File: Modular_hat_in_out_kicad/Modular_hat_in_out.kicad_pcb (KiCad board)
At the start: 2 copper layers, 65 x 56 mm, 146 parts, among them J1 Raspberry_Pi_2_3, U1 MCP3008, U2 LM324, U3 MCP3008, U4 MCP4728, U5 MCP4728, U6 LM324

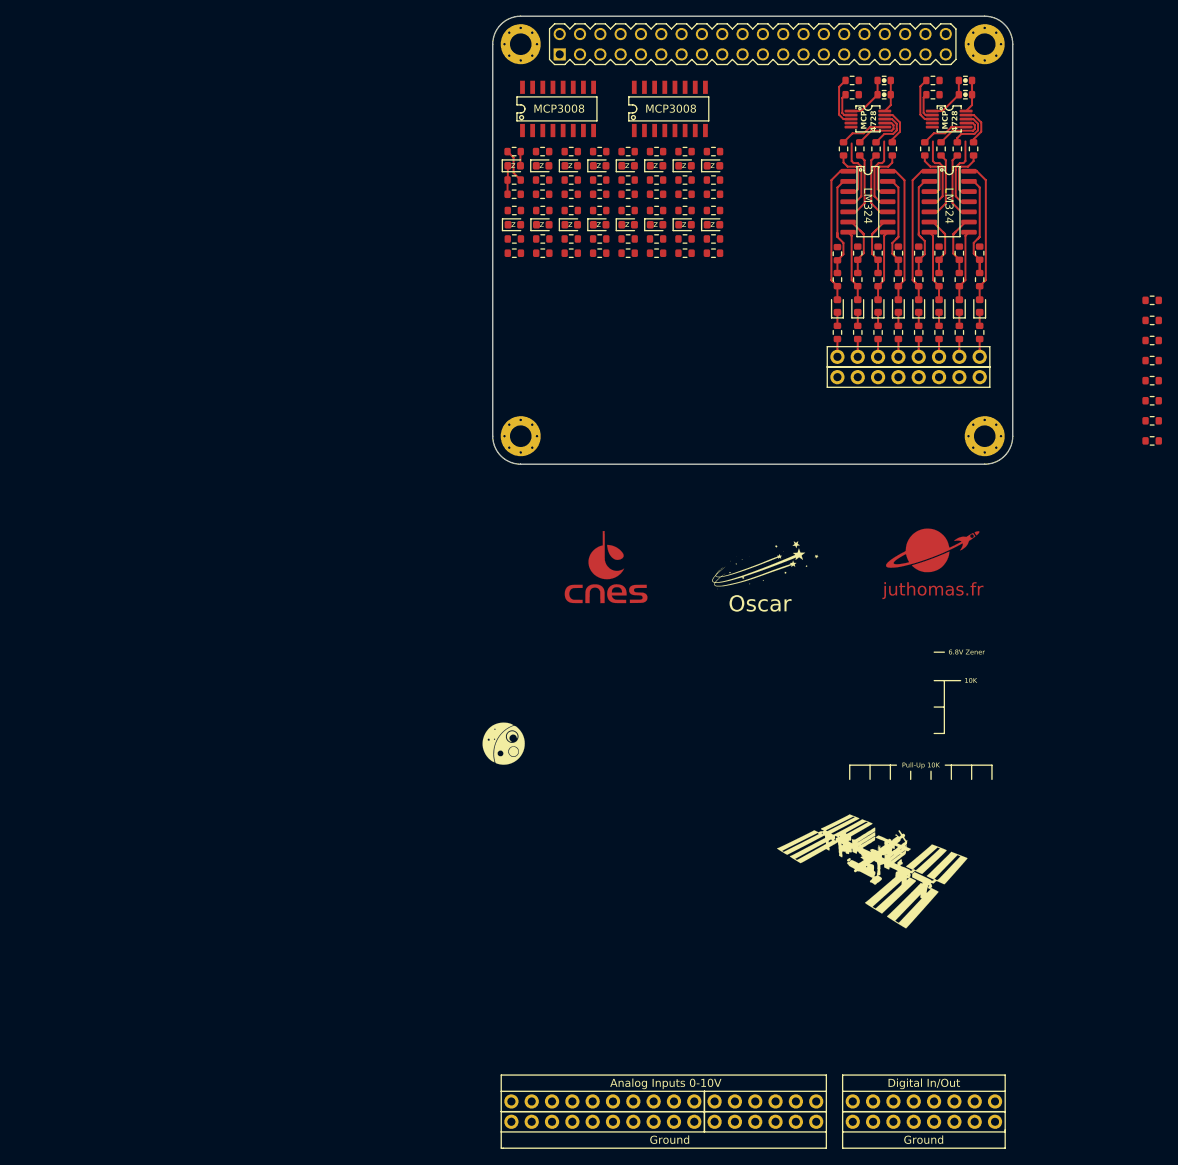
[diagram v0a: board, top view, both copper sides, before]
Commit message: [ADD] Some placements
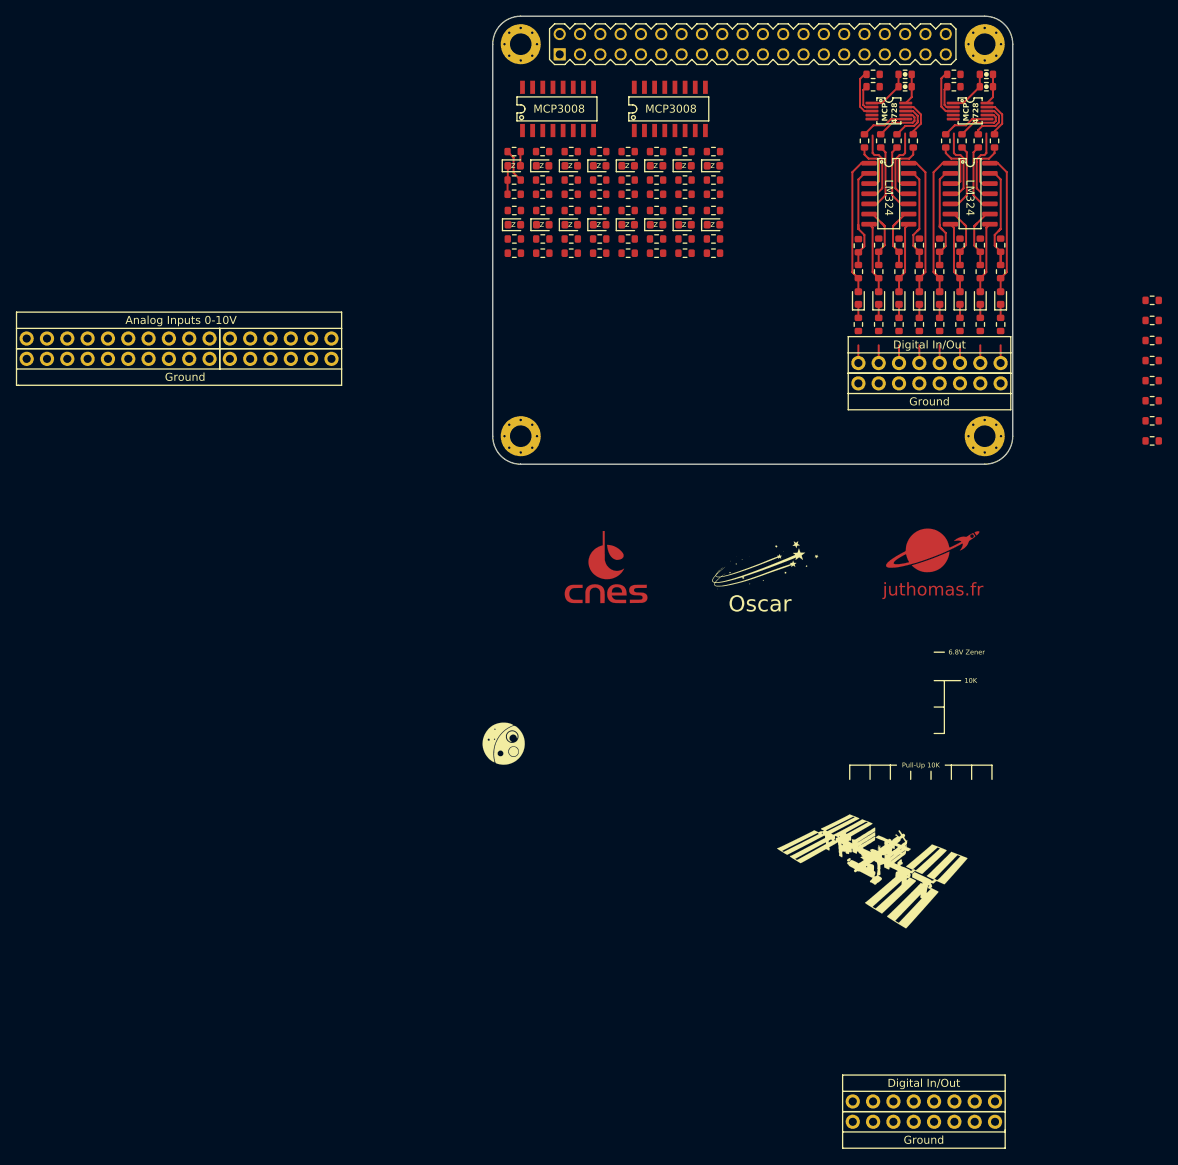
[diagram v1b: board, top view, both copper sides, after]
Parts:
- moved JP1 113.0 mm to (-1.05, 65.5)
- moved JP4 113.0 mm to (-21.4, 65.5)
- moved JP3 113.0 mm to (-1.05, 68.0)
- moved JP6 113.0 mm to (-21.4, 68.0)
- moved C1 2.80 mm to (77.0, 34.0)
- moved C3 2.80 mm to (87.2, 34.0)
- moved D18 2.80 mm to (73.7, 60.4)
- moved D19 2.80 mm to (76.2, 60.4)
- moved D21 2.80 mm to (81.3, 60.4)
- moved D23 2.80 mm to (86.4, 60.4)
- moved R60 2.80 mm to (73.7, 57.1)
- moved R61 2.80 mm to (73.7, 53.8)
- moved R62 2.80 mm to (74.0, 40.8)
- moved R66 2.80 mm to (76.2, 57.1)
- moved R67 2.80 mm to (76.2, 53.8)
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
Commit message: [ADD] Pre routing MCP3008
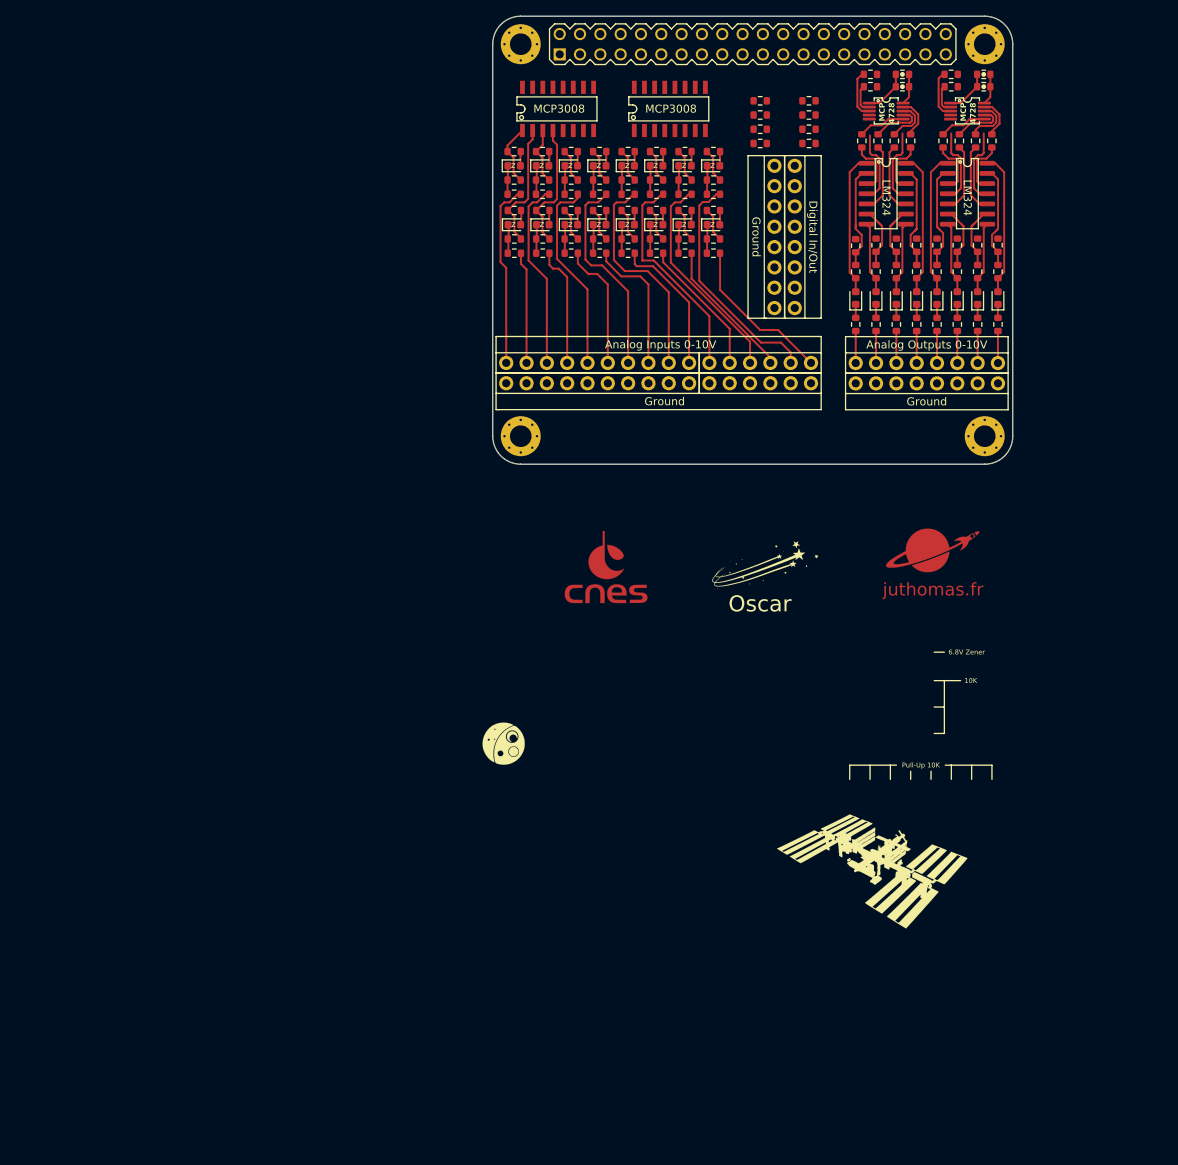
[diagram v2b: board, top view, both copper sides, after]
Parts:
- moved JP2 112.2 mm to (60.7, 52.8), turned to -90 degrees
- moved JP5 109.3 mm to (63.2, 52.8), turned to -90 degrees
- moved R56 63.7 mm to (58.9, 37.6), turned to 180 degrees
- moved R54 61.7 mm to (58.9, 35.8), turned to 180 degrees
- moved JP1 60.0 mm to (58.9, 68.5)
- moved JP3 60.0 mm to (58.9, 71.1)
- moved JP4 60.0 mm to (38.6, 68.5)
- moved JP6 60.0 mm to (38.6, 71.1)
- moved R55 57.5 mm to (65.0, 37.6)
- moved R52 56.0 mm to (58.9, 41.1), turned to 180 degrees
- moved R53 55.4 mm to (65.0, 35.8)
- moved R50 54.5 mm to (58.9, 39.3), turned to 180 degrees
- moved R51 49.5 mm to (65.0, 41.1)
- moved R4 47.9 mm to (65.0, 39.3)
- moved C1 0.33 mm to (76.7, 34.0)
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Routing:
- net /RG14: track 0.00 -> 29.0 mm
- net /RG8: track 0.00 -> 27.4 mm
- net /RG10: track 0.00 -> 27.2 mm
- net /RG12: track 0.00 -> 26.9 mm
- net GND: track 29.1 -> 55.2 mm
- net /RG6: track 0.00 -> 25.9 mm
- net /RG4: track 0.00 -> 24.7 mm
- net /RG2: track 0.00 -> 23.7 mm
- net /RG0: track 0.00 -> 23.0 mm
- net /RG15: track 0.00 -> 19.7 mm
- net /RG13: track 0.00 -> 17.8 mm
- net /RG9: track 0.00 -> 17.7 mm
- net /RG7: track 0.00 -> 17.3 mm
- net /RG11: track 0.00 -> 17.2 mm
- net /CH3: track 0.00 -> 16.2 mm
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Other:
- board text added: "Analog Outputs 0-10V"

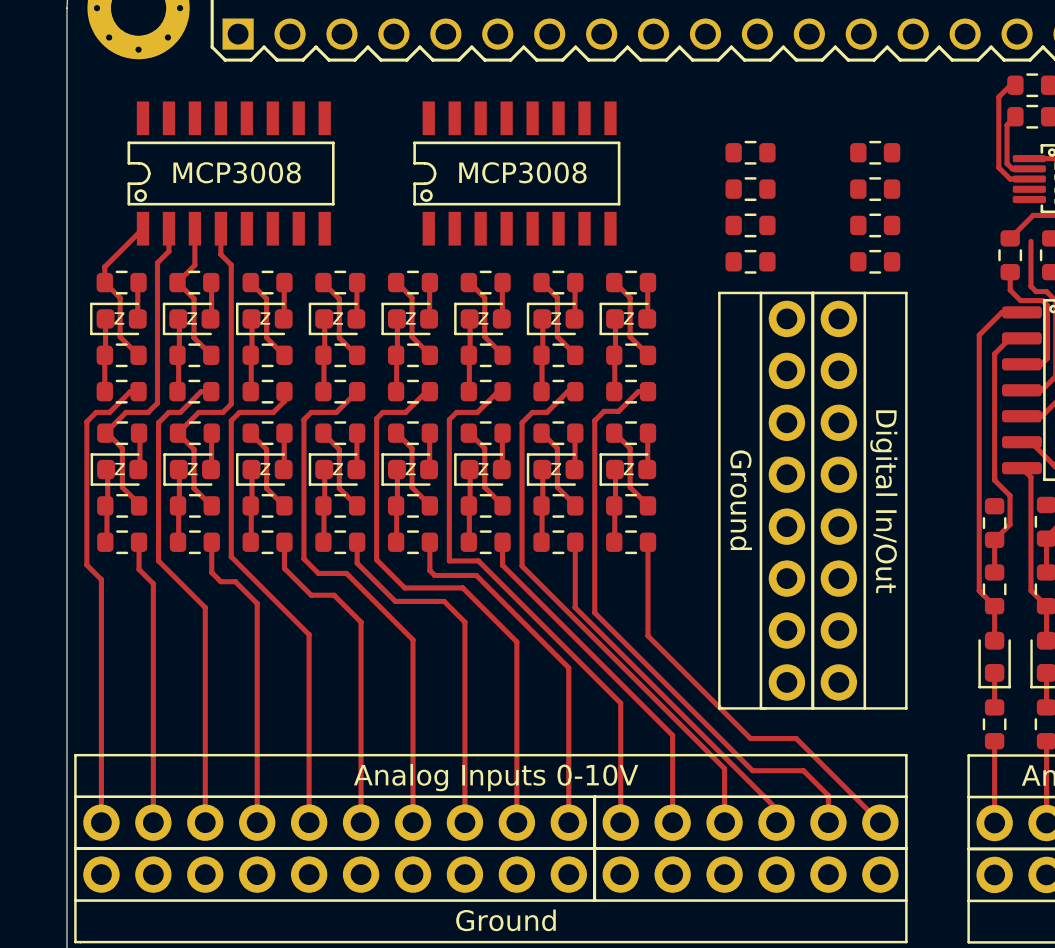
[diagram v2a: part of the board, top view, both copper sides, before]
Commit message: [ADD] Digital routing
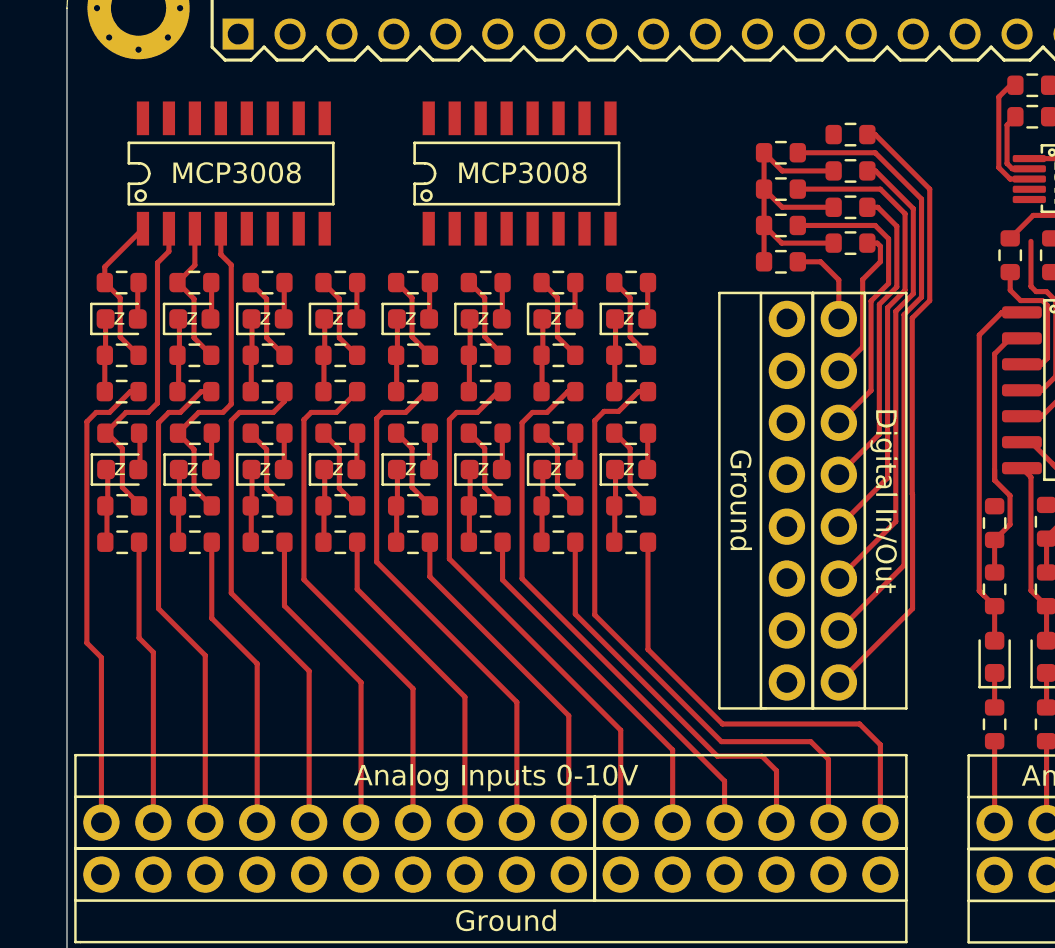
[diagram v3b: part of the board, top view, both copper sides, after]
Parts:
- moved R51 1.51 mm to (63.8, 40.2), turned to 180 degrees
- moved R4 1.50 mm to (63.8, 38.4), turned to 180 degrees
- moved R53 1.50 mm to (63.8, 34.9), turned to 180 degrees
- moved R55 1.50 mm to (63.8, 36.7), turned to 180 degrees
- moved R50 1.49 mm to (60.4, 39.3)
- moved R52 1.49 mm to (60.4, 41.1)
- moved R54 1.49 mm to (60.4, 35.8)
- moved R56 1.49 mm to (60.4, 37.6)
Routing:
- net /D8: track 0.00 -> 30.1 mm
- net /D7: track 0.00 -> 29.8 mm
- net /D6: track 0.00 -> 22.6 mm
- net /D5: track 0.00 -> 22.4 mm
- net /3V3_REG: track 0.00 -> 16.6 mm
- net /D4: track 0.00 -> 15.2 mm
- net /D3: track 0.00 -> 14.7 mm
- net /D2: track 0.00 -> 7.64 mm
- net /D1: track 0.00 -> 4.28 mm
- net /RG15: track 19.7 -> 22.4 mm
- net /RG8: track 27.4 -> 25.8 mm
- net /RG7: track 17.3 -> 15.9 mm
- net /RG13: track 17.8 -> 19.1 mm
- net /RG9: track 17.7 -> 16.5 mm
- net /RG14: track 29.0 -> 30.1 mm
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
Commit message: [ADD] Routing digital
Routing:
- net /GPIO3: track 7.28 -> 83.5 mm
- net /GPIO2: track 12.6 -> 85.6 mm
- net +5V: track 11.9 -> 81.4 mm, vias 0 -> 2
- net /D8: track 30.1 -> 75.1 mm, vias 0 -> 2
- net /D7: track 29.8 -> 72.8 mm, vias 0 -> 2
- net /3V3_REG: track 16.6 -> 58.8 mm, vias 0 -> 2
- net /GPIO11: track 0.00 -> 37.1 mm
- net /D6: track 22.6 -> 57.4 mm
- net /GPIO9: track 0.00 -> 33.6 mm
- net /D5: track 22.4 -> 55.2 mm
- net /GPIO8: track 0.00 -> 28.9 mm
- net /GPIO10: track 0.00 -> 28.7 mm
- net /D4: track 15.2 -> 43.5 mm
- net /D3: track 14.7 -> 39.1 mm
- net /D2: track 7.64 -> 27.7 mm
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
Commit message: [ADD] 12V input in shematics
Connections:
- J1 pad 22: unconnected-(J1-GPIO25-Pad22) -> /GPIO25
- J1 pad 27: unconnected-(J1-ID_SD/GPIO0-Pad27) -> /GPIO0
- J1 pad 28: unconnected-(J1-ID_SC/GPIO1-Pad28) -> /GPIO1
- J1 pad 40: unconnected-(J1-GPIO21/SCLK1-Pad40) -> /GPIO20
- U4 pad 4: Net-(U4-~{LDAC}) -> /GPIO0
- U4 pad 5: Net-(U4-RDY/~{BSY}) -> /GPIO25
- U5 pad 4: Net-(U5-~{LDAC}) -> /GPIO1
- U5 pad 5: Net-(U5-RDY/~{BSY}) -> /GPIO20
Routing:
- net /GPIO1: track 0.00 -> 27.0 mm, vias 0 -> 1
- net /GPIO25: track 0.00 -> 19.1 mm, vias 0 -> 1
- net /GPIO20: track 0.00 -> 13.5 mm, vias 0 -> 1
- net /GPIO0: track 0.00 -> 13.3 mm, vias 0 -> 1

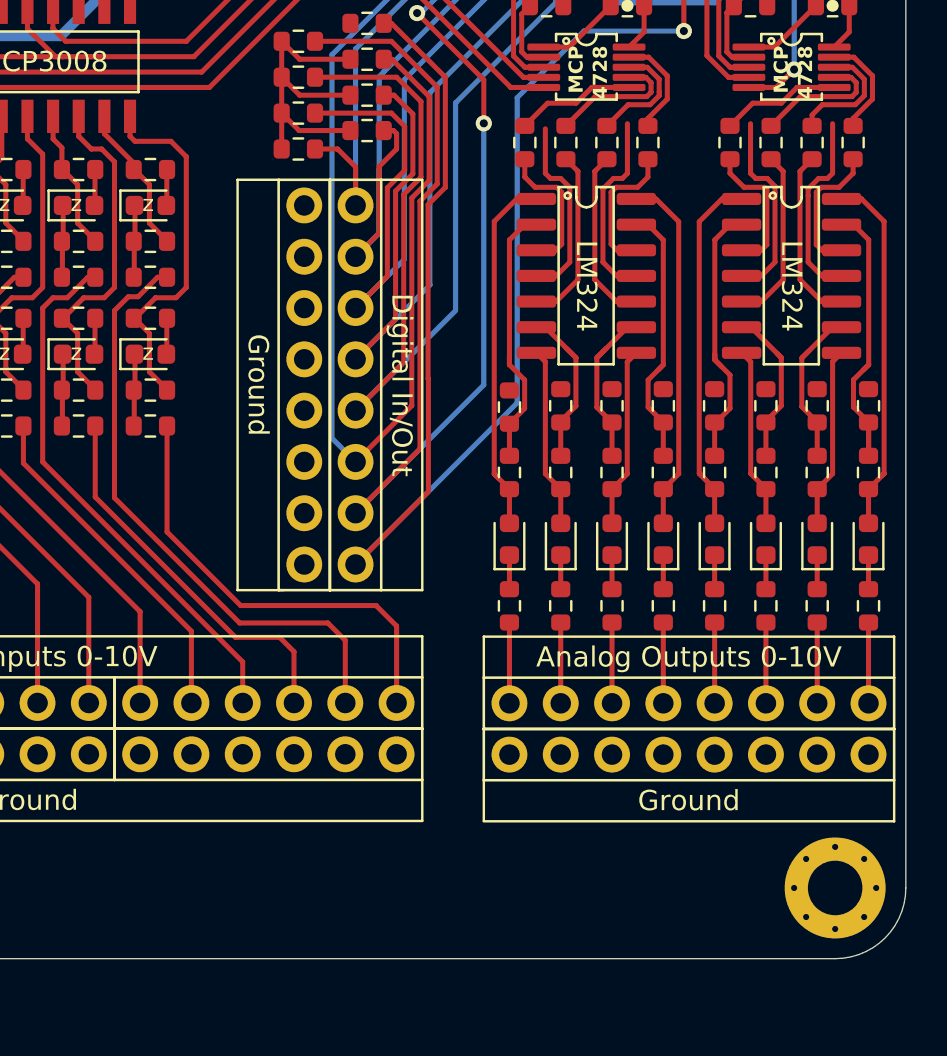
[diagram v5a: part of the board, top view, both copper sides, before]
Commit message: [ADD] All components routed
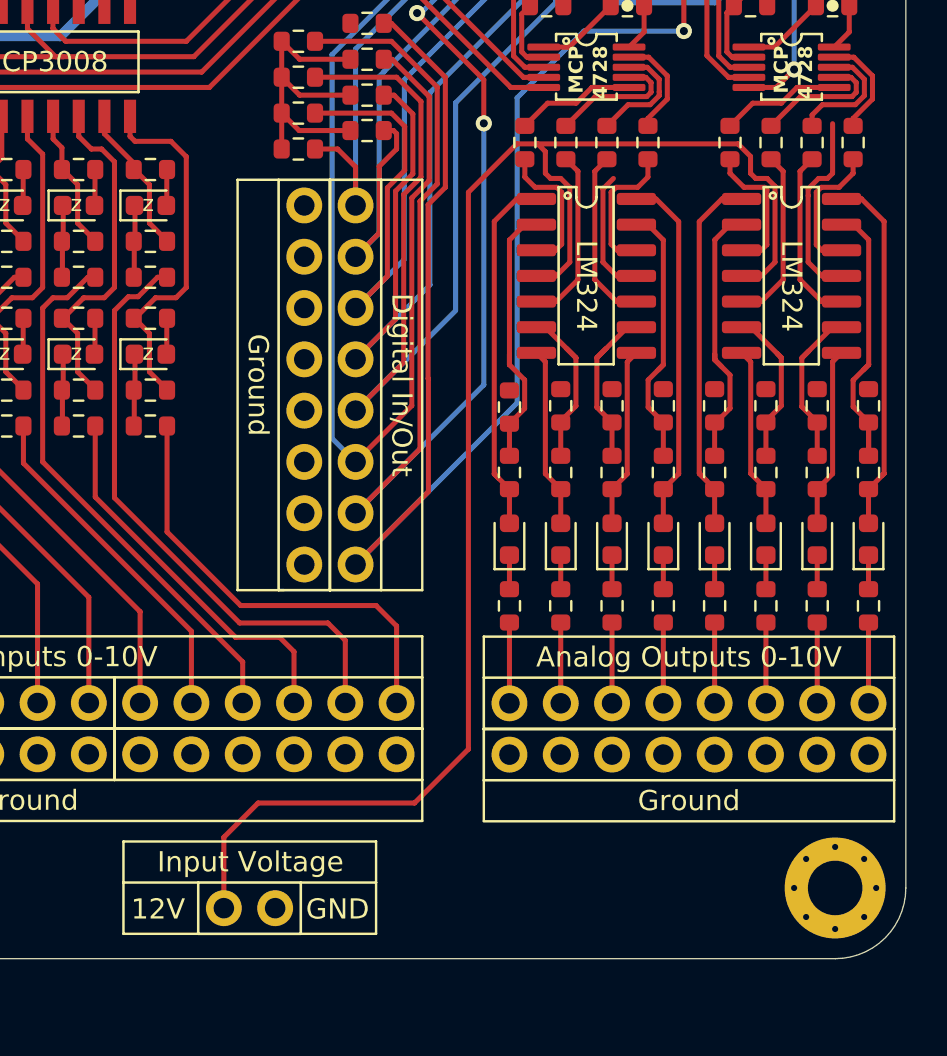
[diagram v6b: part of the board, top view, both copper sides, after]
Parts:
- added JP9: PINHD-1X2, Modular Shield:1X02-BIG, F.Cu at (58.0, 78.7)
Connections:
- U2 pad 4: unconnected-(U2-VCC+-Pad4) -> +12V
- U6 pad 4: unconnected-(U6-VCC+-Pad4) -> +12V
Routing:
- net +12V: track 0.00 -> 77.0 mm
- net unconnected-(U6-VCC+-Pad4): track 9.63 -> 0.00 mm
- net unconnected-(U2-VCC+-Pad4): track 9.34 -> 0.00 mm
- net GND: track 55.2 -> 52.0 mm
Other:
- board text added: "12V"
- board text added: "GND"
- board text added: "Input Voltage"
